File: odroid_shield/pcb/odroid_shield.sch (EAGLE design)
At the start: 71 parts, among them J1 AVRISP6_COMPACT, J4 ODROID_J4, U1 SINGLE-BIT_BUS_TRANSCEIVER, U10 ABM8G, U2 SINGLE-BIT_BUS_TRANSCEIVER, U3 ST1S10, U4 ATMEGA644P-20AU, U5 TS5205, U6 TCA9517MSOP8, U7 MP33926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

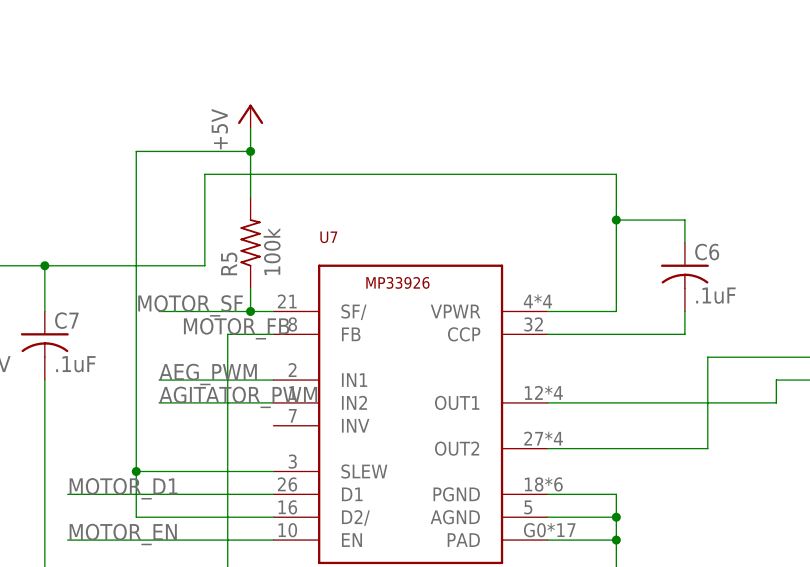
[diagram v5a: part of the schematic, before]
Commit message: Correctly name the motor driver (the correct datasheet was checked in).
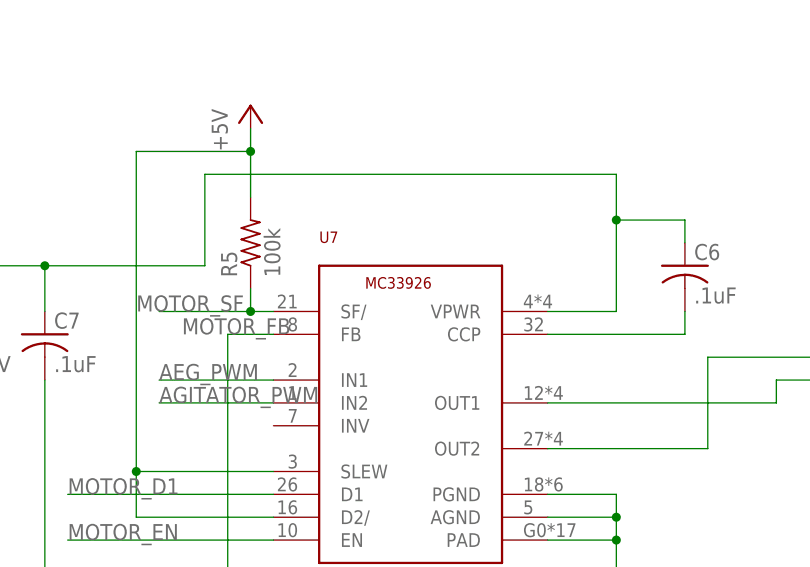
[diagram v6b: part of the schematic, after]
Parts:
- U7: value MP33926 -> MC33926; device odroid_shield:MP33926 -> odroid_shield:MC33926; DPN (none) -> MC33926PNB-ND
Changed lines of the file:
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@@
 <part name="R3" library="rcl" deviceset="R-US_" device="R0603" value="500"/>
 <part name="R4" library="rcl" deviceset="R-US_" device="R0603" value="500"/>
-<part name="U7" library="odroid_shield" deviceset="MP33926" device=""/>
+<part name="U7" library="odroid_shield" deviceset="MC33926" device="">
+<attribute name="DPN" value="MC33926PNB-ND"/>
+</part>
 <part name="C6" library="rcl" deviceset="C-US" device="C0603" value=".1uF"/>
 <part name="R5" library="rcl" deviceset="R-US_" device="R0603" value="100k"/>
@@
 <instance part="R3" gate="G$1" x="17.78" y="154.94" rot="R90"/>
 <instance part="R4" gate="G$1" x="53.34" y="-76.2" rot="R90"/>
-<instance part="U7" gate="G$1" x="109.22" y="149.86"/>
+<instance part="U7" gate="G$1" x="109.22" y="149.86">
+<attribute name="DPN" x="109.22" y="149.86" size="1.778" layer="96" display="off"/>
+</instance>
 <instance part="C6" gate="G$1" x="139.7" y="165.1"/>
 <instance part="R5" gate="G$1" x="91.44" y="167.64" rot="R90"/>

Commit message: odroid_shield: Updates after pre-mfg checks from macrofab.
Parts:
- C11, C12: value 20pF -> 22pF
- C4: device rcl:C-USC1206 -> rcl:C-USC1210
- L1: value 33uH -> 3.3uH
- R10, R7, R8, R9: value 4.7k -> 5.6k
- R11, R6: value 200 -> 220
- R3, R4: value 500 -> 560
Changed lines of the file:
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@@
 <attribute name="DPN" value="CMS06QMCT-ND"/>
 </part>
-<part name="C4" library="rcl" deviceset="C-US" device="C1206" value="22uF 16V">
+<part name="C4" library="rcl" deviceset="C-US" device="C1210" value="22uF 16V">
 <attribute name="DPN" value="445-3955-1-ND"/>
 </part>
-<part name="L1" library="odroid_shield" deviceset="L-US" device="WURTH_74404042033" value="33uH">
+<part name="L1" library="odroid_shield" deviceset="L-US" device="WURTH_74404042033" value="3.3uH">
 <attribute name="DPN" value="732-5505-1-ND"/>
 </part>
@@
 <attribute name="DPN" value="445-3955-1-ND"/>
 </part>
-<part name="R3" library="rcl" deviceset="R-US_" device="R0603" value="500"/>
-<part name="R4" library="rcl" deviceset="R-US_" device="R0603" value="500"/>
+<part name="R3" library="rcl" deviceset="R-US_" device="R0603" value="560"/>
+<part name="R4" library="rcl" deviceset="R-US_" device="R0603" value="560"/>
 <part name="U7" library="odroid_shield" deviceset="MC33926" device="">
 <attribute name="DPN" value="MC33926PNB-ND"/>
@@
 <part name="R5" library="rcl" deviceset="R-US_" device="R0603" value="100k"/>
 <part name="P+5" library="supply1" deviceset="+5V" device=""/>
-<part name="R6" library="rcl" deviceset="R-US_" device="R0603" value="200"/>
+<part name="R6" library="rcl" deviceset="R-US_" device="R0603" value="220"/>
 <part name="U5" library="v-reg" deviceset="TS5205" device=""/>
 <part name="GND9" library="supply1" deviceset="GND" device=""/>
@@
 <part name="Q1" library="zetex" deviceset="NMOSSOT23" device=""/>
 <part name="U6" library="odroid_shield" deviceset="TCA9517" device="MSOP8"/>
-<part name="R7" library="rcl" deviceset="R-US_" device="R0603" value="4.7k"/>
-<part name="R8" library="rcl" deviceset="R-US_" device="R0603" value="4.7k"/>
-<part name="R9" library="rcl" deviceset="R-US_" device="R0603" value="4.7k"/>
-<part name="R10" library="rcl" deviceset="R-US_" device="R0603" value="4.7k"/>
+<part name="R7" library="rcl" deviceset="R-US_" device="R0603" value="5.6k"/>
+<part name="R8" library="rcl" deviceset="R-US_" device="R0603" value="5.6k"/>
+<part name="R9" library="rcl" deviceset="R-US_" device="R0603" value="5.6k"/>
+<part name="R10" library="rcl" deviceset="R-US_" device="R0603" value="5.6k"/>
 <part name="U4" library="odroid_shield" deviceset="ATMEGA644P-20AU" device=""/>
 <part name="GND10" library="supply1" deviceset="GND" device=""/>
@@
 <part name="GND12" library="supply1" deviceset="GND" device=""/>
 <part name="P+9" library="supply1" deviceset="+5V" device=""/>
-<part name="R11" library="rcl" deviceset="R-US_" device="R0603" value="200"/>
+<part name="R11" library="rcl" deviceset="R-US_" device="R0603" value="220"/>
 <part name="U10" library="odroid_shield" deviceset="ABM8G" device="">
 <attribute name="DPN" value="535-10267-6-ND"/>
 </part>
 <part name="GND13" library="supply1" deviceset="GND" device=""/>
-<part name="C11" library="rcl" deviceset="C-US" device="C0603" value="20pF"/>
-<part name="C12" library="rcl" deviceset="C-US" device="C0603" value="20pF"/>
+<part name="C11" library="rcl" deviceset="C-US" device="C0603" value="22pF"/>
+<part name="C12" library="rcl" deviceset="C-US" device="C0603" value="22pF"/>
 <part name="GND14" library="supply1" deviceset="GND" device=""/>
 <part name="+3V3" library="supply1" deviceset="+3V3" device=""/>
